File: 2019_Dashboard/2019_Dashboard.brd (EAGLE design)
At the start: 93.7 x 53 mm, 61 parts, among them IC1 MCP23017SO, Q1 TN0602N3, Q2 TN0602N3, Q3 TN0602N3, Q4 TN0602N3, Q5 TN0602N3, U1 TLC59281, Y1 16MHz

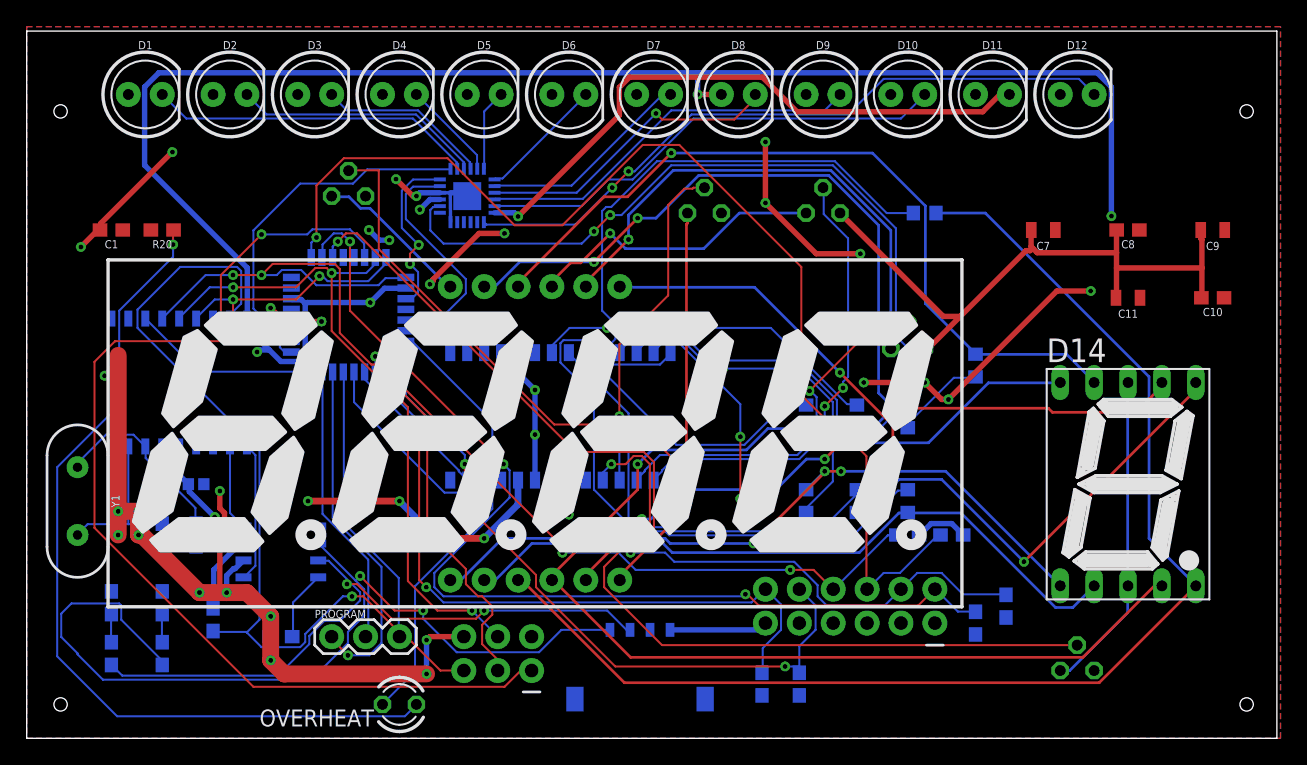
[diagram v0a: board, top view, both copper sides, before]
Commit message: Updated dashboard schematic, fix post-order bugs
Board not updated yet
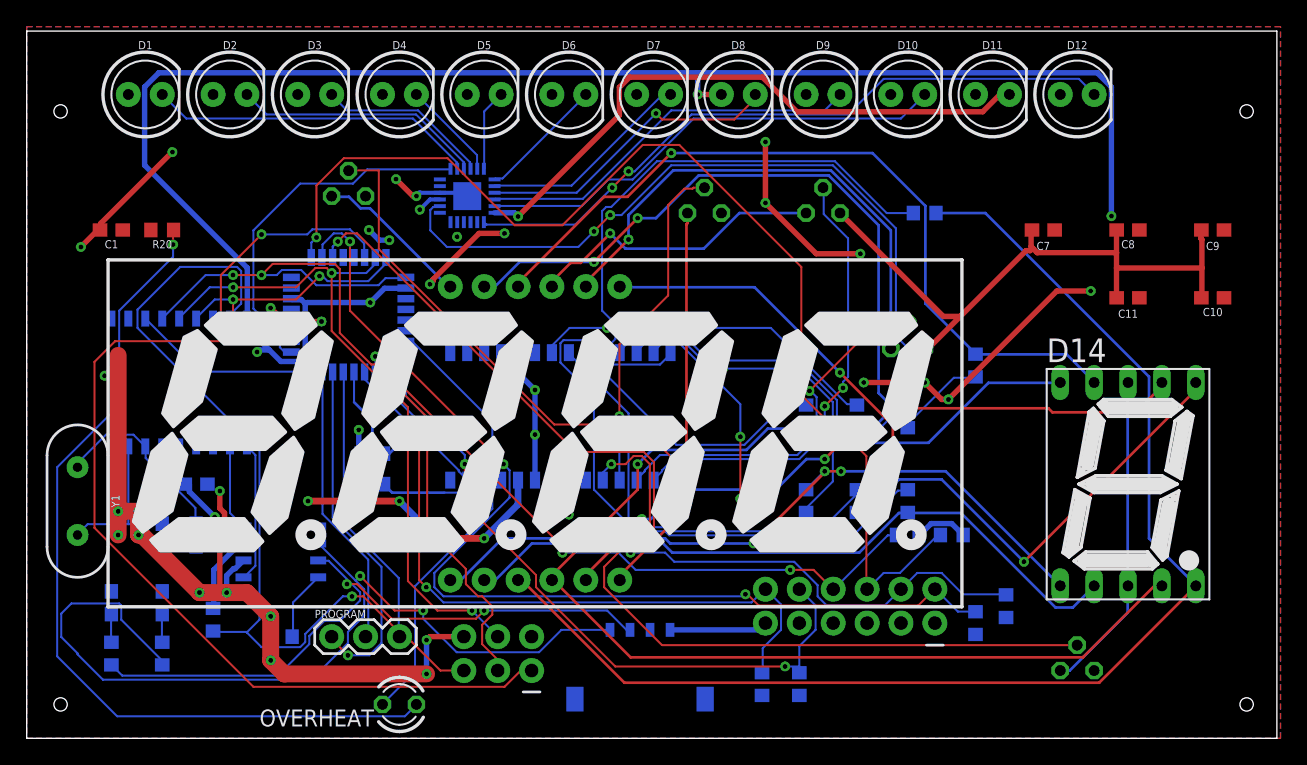
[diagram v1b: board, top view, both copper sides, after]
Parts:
- added R7, R8: 4.7k, rcl:R0603
- C1, C10, C2, C3, C4, C5, C8: device SparkFun-Capacitors:0603 -> rcl:C0603
- C11, C7, C9: device SparkFun-Capacitors:0805 -> rcl:C0603
- C6: device SparkFun-Capacitors:0402 -> rcl:C0603
- CANH, CANL, R20, R22: device SparkFun-Resistors:0603 -> rcl:R0603
- R1, R2, R3, R4, R5, R6: value 1k -> 4.7k; device SparkFun-Resistors:0603 -> rcl:R0603
- R13, R14, R16, R17, R18, R19, R23: value 330 -> 180; device resistor:R0603 -> rcl:R0603
- R15: value 330 -> 180\; device resistor:R0603 -> rcl:R0603
- R21: value 10k -> 4.7k; device SparkFun-Resistors:0603 -> rcl:R0603
- R24: device resistor:R0603 -> rcl:R0603
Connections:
- net N$20 renamed LATCH
- removed net N$18: CONTROL.19, U1.24
- removed net N$19: CONTROL.22, U1.23
- new net BLANK: CONTROL.2, U1.18
- new net SCLK: CONTROL.8, U1.24
- new net SIN: CONTROL.7, U1.23
- net GND: now also C2.2, C3.2; no longer C2.1, C3.1, U1.18
- net N$1: now also R8.1
- net N$2: now also R7.1
- net OSC1: now also C2.1; no longer C2.2
- net OSC2: now also C3.1; no longer C3.2
- net VCC: now also R7.2, R8.2
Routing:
- net N$19: track 17.8 -> 0.00 mm
- net N$18: track 13.0 -> 0.00 mm, vias 2 -> 0
- net VCC: track 163.9 -> 168.1 mm, vias 11 -> 12
- net N$2: track 11.4 -> 14.5 mm
- net N$1: track 15.3 -> 17.6 mm
- net GND: track 202.2 -> 200.0 mm
- net OSC2: track 14.0 -> 15.7 mm
- net OSC1: track 12.6 -> 14.2 mm
